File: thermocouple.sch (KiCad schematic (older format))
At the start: 8 parts, among them U1 MAX31855KASA

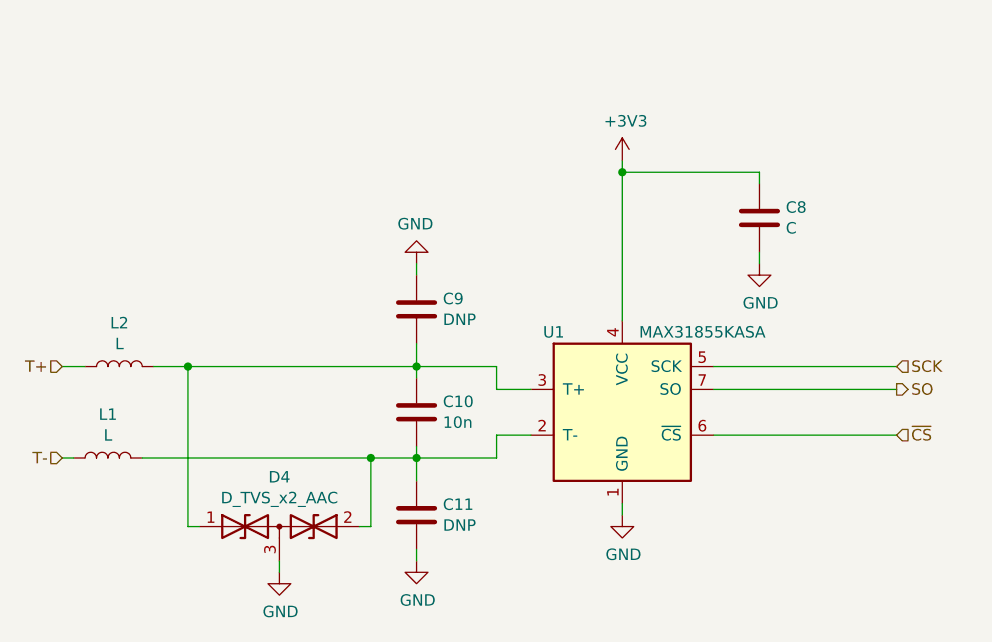
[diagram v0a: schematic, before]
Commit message: 見つけた設計ミスを全部反映
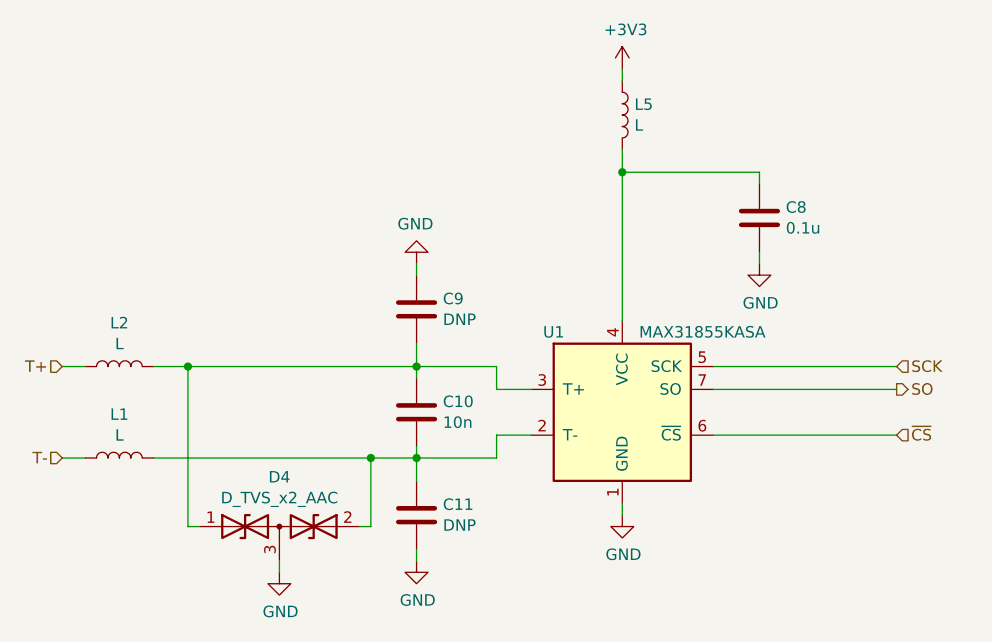
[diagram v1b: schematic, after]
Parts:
- added L5: L, Inductor_SMD:L_0603_1608Metric, symbol Device:L
- C8: value C -> 0.1u
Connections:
- net +3V3: now also L5.1; no longer C8.1, U1.4 (VCC)
- new net: C8.1, L5.2, U1.4 (VCC)
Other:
- moved on the sheet: L1
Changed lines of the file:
@@
 EESchema Schematic File Version 4
-LIBS:Encoder_check-cache
 EELAYER 30 0
 EELAYER END
@@
 P 6100 3000
 F 0 "C8" H 6215 3046 50  0000 L CNN
-F 1 "C" H 6215 2955 50  0000 L CNN
+F 1 "0.1u" H 6215 2955 50  0000 L CNN
 F 2 "Capacitor_SMD:C_0603_1608Metric" H 6138 2850 50  0001 C CNN
 F 3 "~" H 6100 3000 50  0001 C CNN
@@
 L power:+3V3 #PWR0127
 U 1 1 5E2BAEF8
-P 5500 2750
-F 0 "#PWR0127" H 5500 2600 50  0001 C CNN
-F 1 "+3V3" H 5515 2923 50  0000 C CNN
-F 2 "" H 5500 2750 50  0001 C CNN
-F 3 "" H 5500 2750 50  0001 C CNN
-	1    5500 2750
-	1    0    0    -1
-$EndComp
-Wire Wire Line
-	5500 2750 5500 2800
+P 5500 2350
+F 0 "#PWR0127" H 5500 2200 50  0001 C CNN
+F 1 "+3V3" H 5515 2523 50  0000 C CNN
+F 2 "" H 5500 2350 50  0001 C CNN
+F 3 "" H 5500 2350 50  0001 C CNN
+	1    5500 2350
+	1    0    0    -1
+$EndComp
+Wire Wire Line
+	5500 2350 5500 2400
 Connection ~ 5500 2800
 Wire Wire Line
@@
 L Device:L L?
 U 1 1 5E2E4AB1
-P 3250 4050
+P 3300 4050
 AR Path="/5E2E4AB1" Ref="L?"  Part="1"
 AR Path="/5E34C60F/5E2E4AB1" Ref="L1"  Part="1"
-F 0 "L1" V 3440 4050 50  0000 C CNN
-F 1 "L" V 3349 4050 50  0000 C CNN
-F 2 "Inductor_SMD:L_0603_1608Metric" H 3250 4050 50  0001 C CNN
-F 3 "~" H 3250 4050 50  0001 C CNN
-	1    3250 4050
+F 0 "L1" V 3490 4050 50  0000 C CNN
+F 1 "L" V 3399 4050 50  0000 C CNN
+F 2 "Inductor_SMD:L_0603_1608Metric" H 3300 4050 50  0001 C CNN
+F 3 "~" H 3300 4050 50  0001 C CNN
+	1    3300 4050
 	0    -1   -1   0
 $EndComp
 Wire Wire Line
-	3400 4050 4400 4050
+	3450 4050 4400 4050
 Connection ~ 4600 4050
 Wire Wire Line
 	3050 3650 3150 3650
 Wire Wire Line
-	3050 4050 3100 4050
+	3050 4050 3150 4050
 Wire Wire Line
 	4950 3650 4950 3750
@@
 Wire Wire Line
 	3600 3650 4600 3650
+$Comp
+L Device:L L5
+U 1 1 5E54FD55
+P 5500 2550
+F 0 "L5" H 5553 2596 50  0000 L CNN
+F 1 "L" H 5553 2505 50  0000 L CNN
+F 2 "Inductor_SMD:L_0603_1608Metric" H 5500 2550 50  0001 C CNN
+F 3 "~" H 5500 2550 50  0001 C CNN
+	1    5500 2550
+	1    0    0    -1
+$EndComp
+Wire Wire Line
+	5500 2700 5500 2800
 $EndSCHEMATC
